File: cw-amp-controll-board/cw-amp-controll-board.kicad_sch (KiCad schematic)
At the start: 54 parts, among them J1 Conn_02x07_Odd_Even, J2 Conn_01x06, J3 Conn_02x05_Odd_Even, J5 Conn_01x02, Q1 BC850, Q2 BC850, Q3 BC850, Q4 BC850, SW1 RotaryEncoder_Switch, U1 LDL1117S33R, U2 PCF8574, U3 ESP32-C3-WROOM-02, U4 AT42QT2120-CommsMode, U5 PCF8574

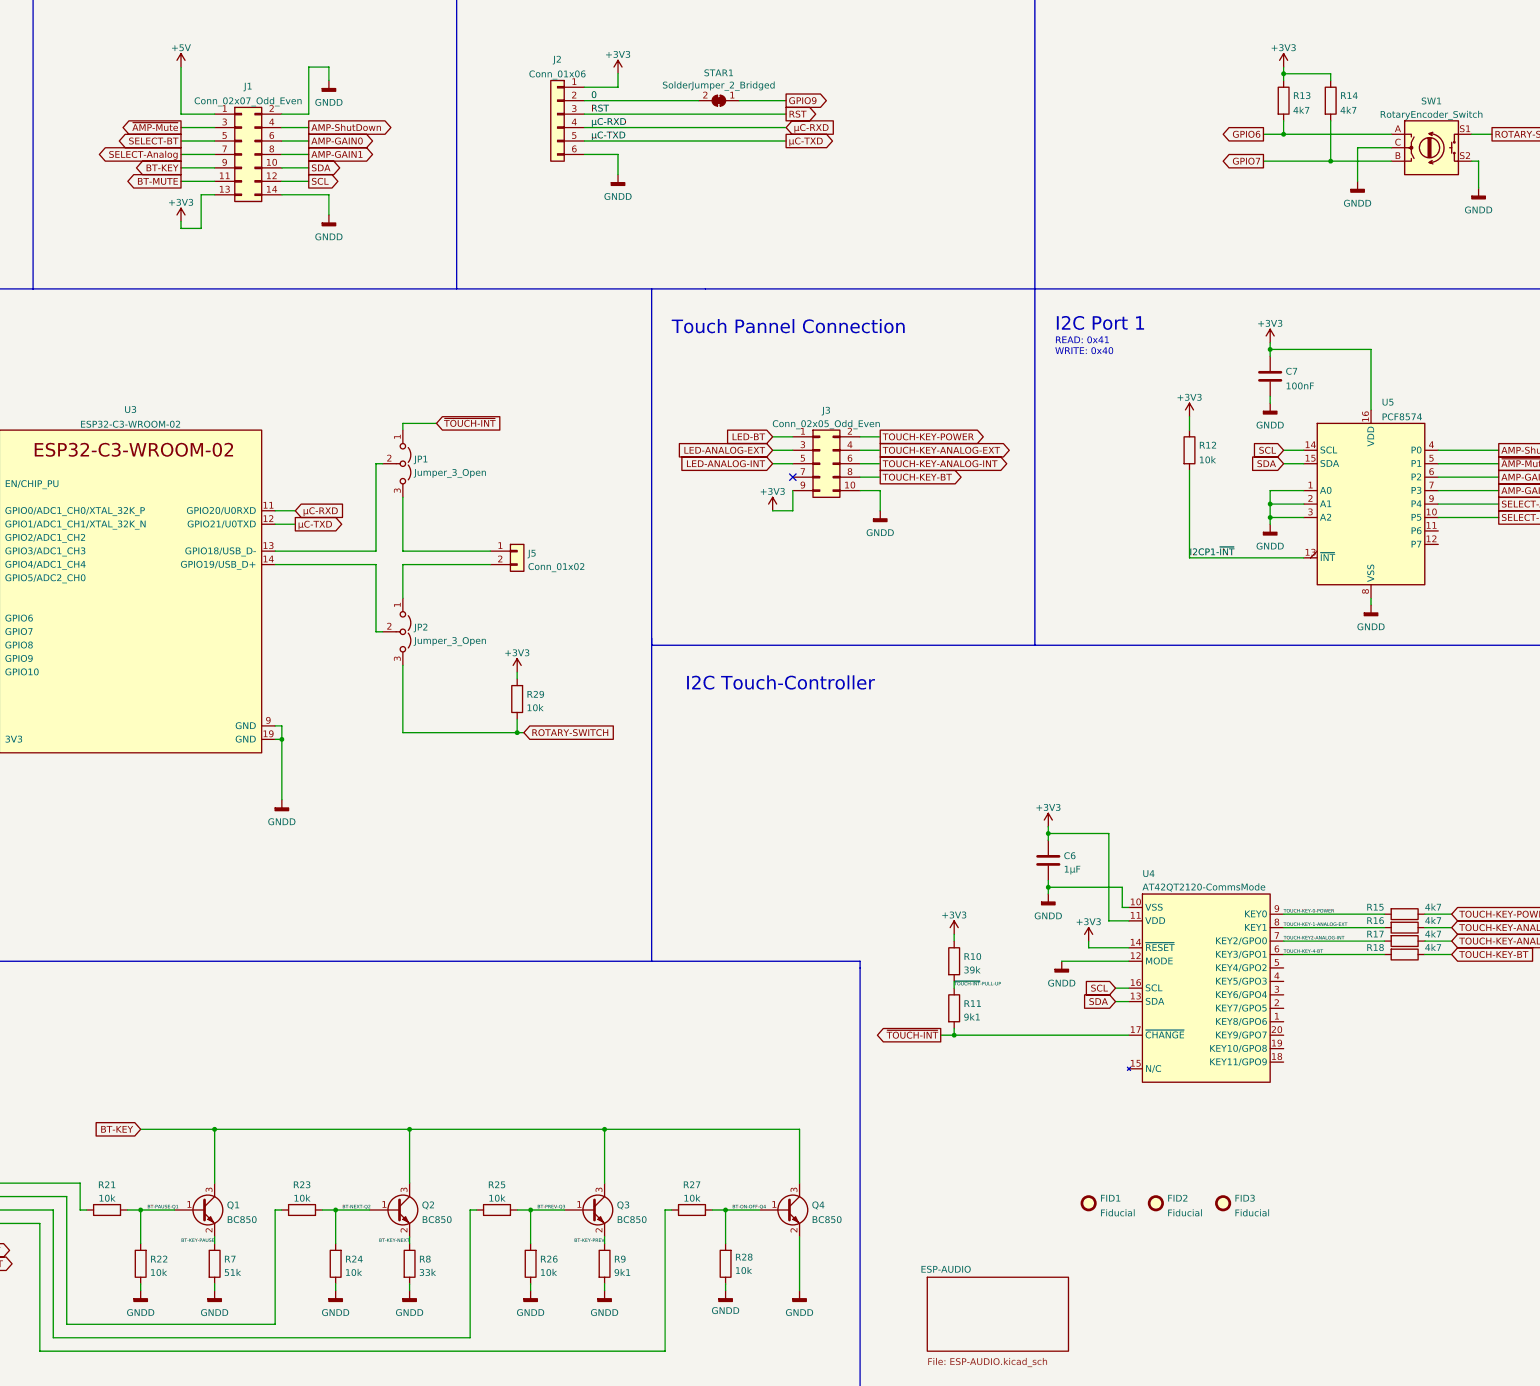
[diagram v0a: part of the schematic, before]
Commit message: reqork for 1.2, fix error with i2c port expander
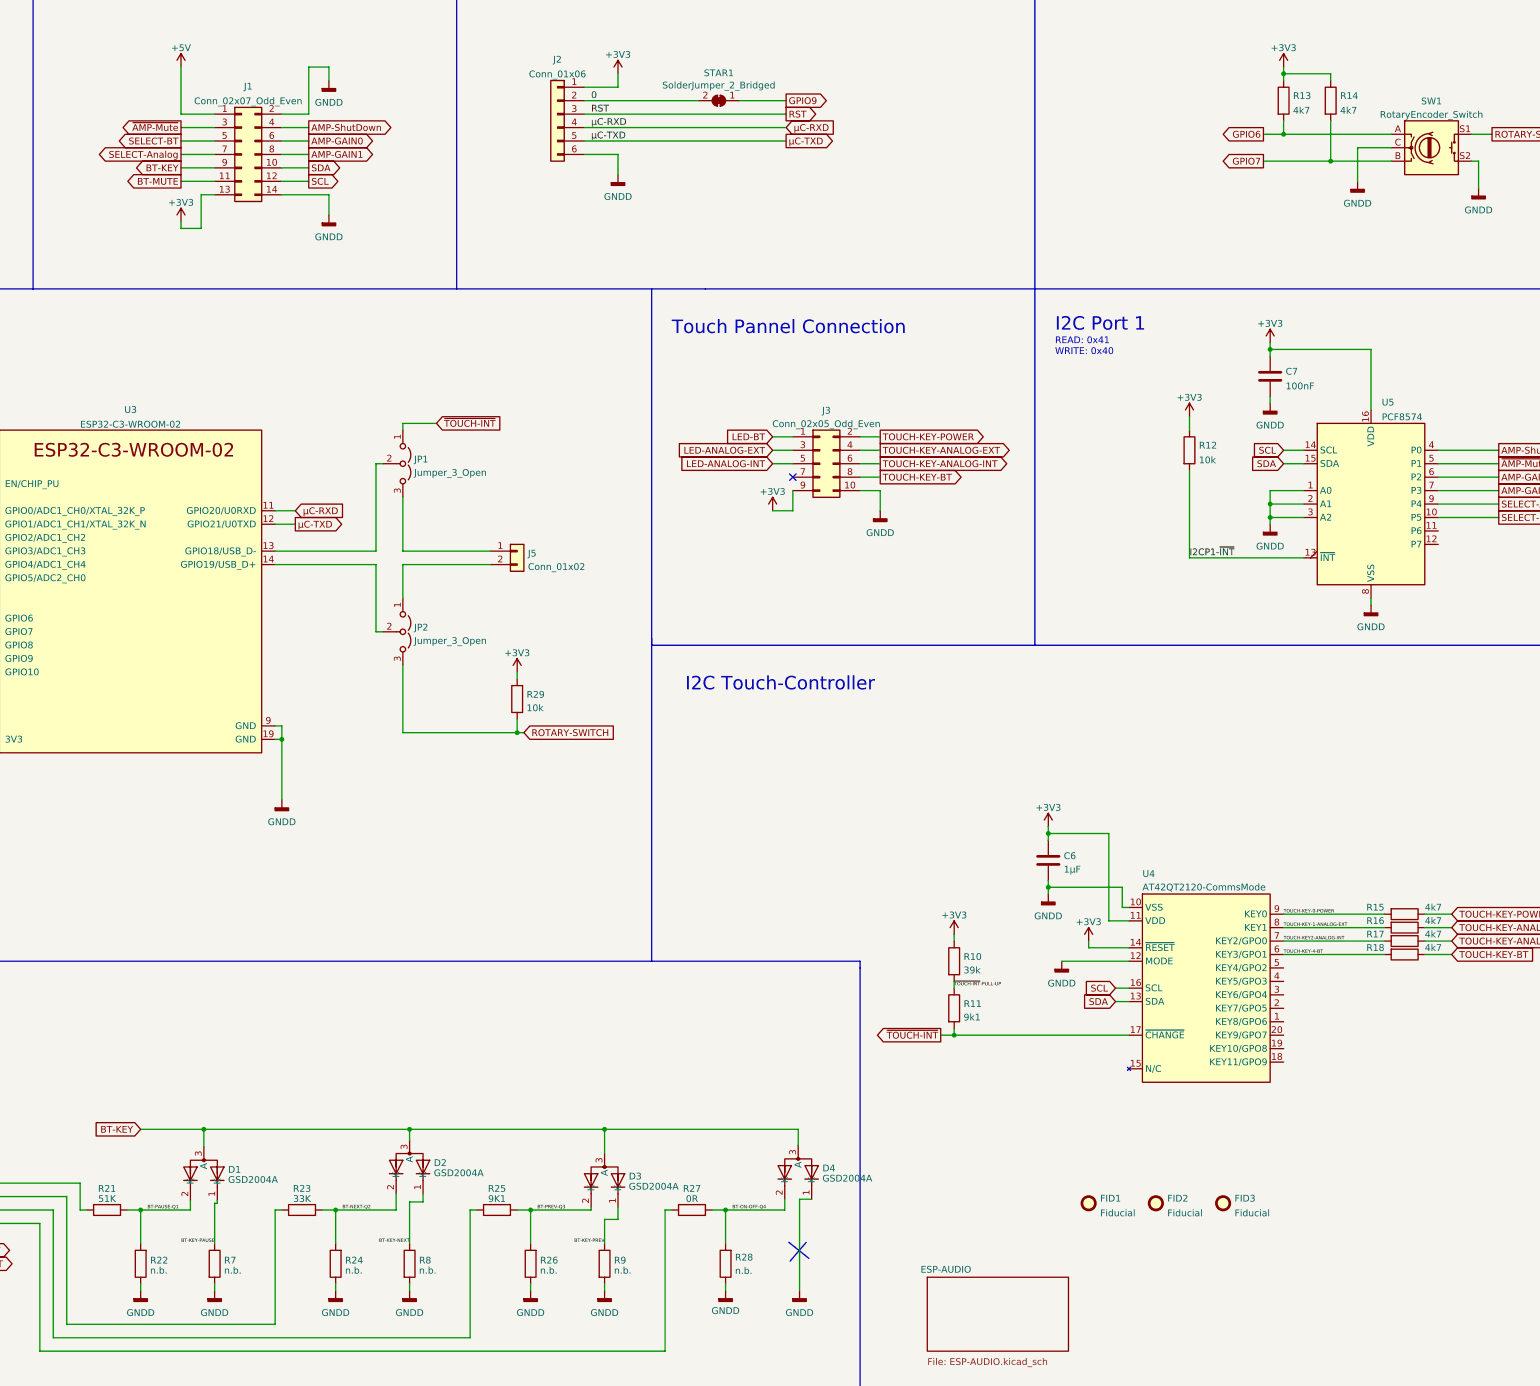
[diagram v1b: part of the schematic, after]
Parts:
- removed Q1, Q2, Q3, Q4: BC850, Package_TO_SOT_SMD:SOT-23, symbol Transistor_BJT:BC850
- added D1, D2, D3, D4: GSD2004A, Package_TO_SOT_SMD:SOT-23, symbol office amp:GSD2004A
- R21: value 10k -> 51K
- R22, R24, R26, R28: value 10k -> n.b.
- R23: value 10k -> 33K
- R25: value 10k -> 9K1
- R27: value 10k -> 0R
- R7: value 51k -> n.b.
- R8: value 33k -> n.b.
- R9: value 9k1 -> n.b.
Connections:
- net BT-KEY: now also D1.3 (A), D2.3 (A), D3.3 (A), D4.3 (A)
- net BT-KEY-NEXT: now also D2.1 (K)
- net BT-KEY-PAUSE: now also D1.1 (K)
- net BT-KEY-PREV: now also D3.1 (K)
- net BT-NEXT-Q2: now also D2.2 (K)
- net BT-ON-OFF-Q4: now also D4.2 (K)
- net BT-PAUSE-Q1: now also D1.2 (K)
- net BT-PREV-Q3: now also D3.2 (K)
- net GNDD: now also D4.1 (K)

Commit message: Added outputdriver and fixed bug with i2c port expander
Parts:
- removed D1, D2, D3, D4: GSD2004A, Package_TO_SOT_SMD:SOT-23, symbol office amp:GSD2004A
- removed R22, R24, R26, R28, R7, R8, R9: n.b., Resistor_SMD:R_0805_2012Metric_Pad1.20x1.40mm_HandSolder, symbol Device:R
- added C19: 100nF, Capacitor_SMD:C_0805_2012Metric_Pad1.18x1.45mm_HandSolder, symbol Device:C
- added U7: 7400, symbol 74xx:7400
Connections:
- net BT-NEXT-Q2 is gone; now on net BT-KEY: R23.2
- net BT-ON-OFF-Q4 is gone; now on net BT-KEY: R27.2
- net BT-PAUSE-Q1 is gone; now on net BT-KEY: R21.2
- net BT-PREV-Q3 is gone; now on net BT-KEY: R25.2
- net +5V: now also C19.1, U7.12, U7.13, U7.14 (VCC)
- net GNDD: now also C19.2, U7.7 (GND)
- net SELECT-Analog: now also U7.6; no longer U5.9 (P4)
- net SELECT-BT: now also U7.8; no longer U5.10 (P5)
- net ~{AMP-Mute}: now also U7.3; no longer U5.5 (P1)
- new net AMP-MUTE: U5.5 (P1), U7.1, U7.2
- new net ~{SELECT-Analog}: U5.9 (P4), U7.4, U7.5
- new net ~{SELECT-BT}: U5.10 (P5), U7.10, U7.9
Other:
- note added: "Output Driver Supply"
- moved on the sheet: C6, C7, R10, R11, R12, R15, R16, R17, R18, R21, R23, R25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

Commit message: layout v1.2
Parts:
- U7: footprint (none) -> Package_SO:SOIC-14_3.9x8.7mm_P1.27mm
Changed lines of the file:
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@@
   (symbol (lib_id "power:GNDD") (at 281.94 176.53 0) (unit 1)
     (in_bom yes) (on_board yes) (dnp no) (fields_autoplaced)
-    (property "Reference" "#PWR?" (at 281.94 182.88 0)
+    (property "Reference" "#PWR0101" (at 281.94 182.88 0)
       (effects (font (size 1.27 1.27)) hide)
     )
@@
       (project "cw-amp-controll-board"
         (path "/b317c2a8-aef2-47e1-872b-e524d2763beb"
-          (reference "#PWR?") (unit 1)
+          (reference "#PWR0101") (unit 1)
         )
       )
@@
       (effects (font (size 1.27 1.27)))
     )
-    (property "Footprint" "" (at 234.95 238.76 0)
+    (property "Footprint" "Package_SO:SOIC-14_3.9x8.7mm_P1.27mm" (at 234.95 238.76 0)
       (effects (font (size 1.27 1.27)) hide)
     )
@@
       (effects (font (size 1.27 1.27)))
     )
-    (property "Footprint" "" (at 372.11 108.585 0)
+    (property "Footprint" "Package_SO:SOIC-14_3.9x8.7mm_P1.27mm" (at 372.11 108.585 0)
       (effects (font (size 1.27 1.27)) hide)
     )
@@
       (effects (font (size 1.27 1.27)))
     )
-    (property "Footprint" "" (at 234.95 263.525 0)
+    (property "Footprint" "Package_SO:SOIC-14_3.9x8.7mm_P1.27mm" (at 234.95 263.525 0)
       (effects (font (size 1.27 1.27)) hide)
     )
@@
       (effects (font (size 1.27 1.27)) (justify left))
     )
-    (property "Footprint" "" (at 334.01 109.22 0)
+    (property "Footprint" "Package_SO:SOIC-14_3.9x8.7mm_P1.27mm" (at 334.01 109.22 0)
       (effects (font (size 1.27 1.27)) hide)
     )
@@
       (effects (font (size 1.27 1.27)))
     )
-    (property "Footprint" "" (at 234.95 251.46 0)
-      (effects (font (size 1.27 1.27)) hide)
-    )
+    (property "Footprint" "Package_SO:SOIC-14_3.9x8.7mm_P1.27mm" (at 234.95 251.46 0)
+      (effects (font (size 1.27 1.27)) hide)
+    )
